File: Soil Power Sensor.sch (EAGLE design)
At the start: 91 parts, among them J1 12401832E402A, U10 TPS7A20330PDBVR, U11 TPS60403DBVR, U12 REF1933AIDDCR, U13 TLV1117LV33DCYR, U14 FSA2466UMX, U2 FT234XD-R, U3 MAX9944ATA+T, U4 ESP32-C3-MINI-1-N4, U5 LTC6362CDDPBF, U6 LTC6362CDDPBF, U7 INA296A5, U8 MAX11201AEUB+, U9 MAX11201AEUB+, X1 SMA-142-0701-801/806

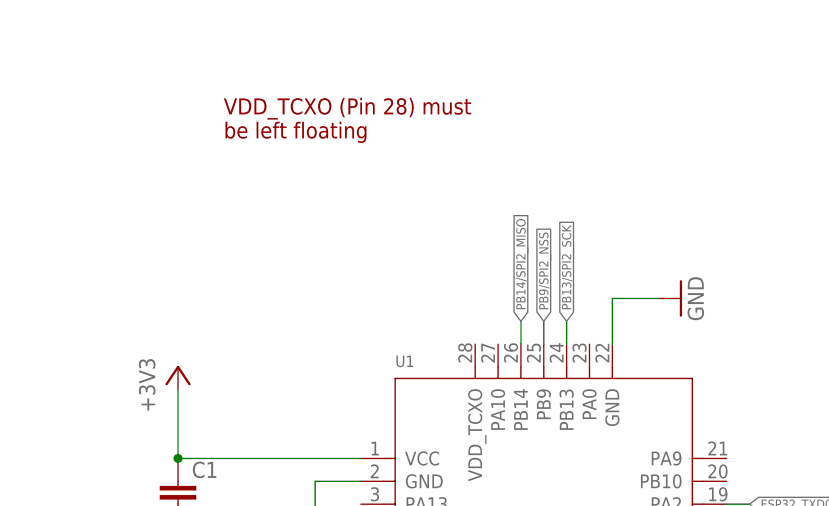
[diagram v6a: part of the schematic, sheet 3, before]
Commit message: Added voltage monitoring circuit
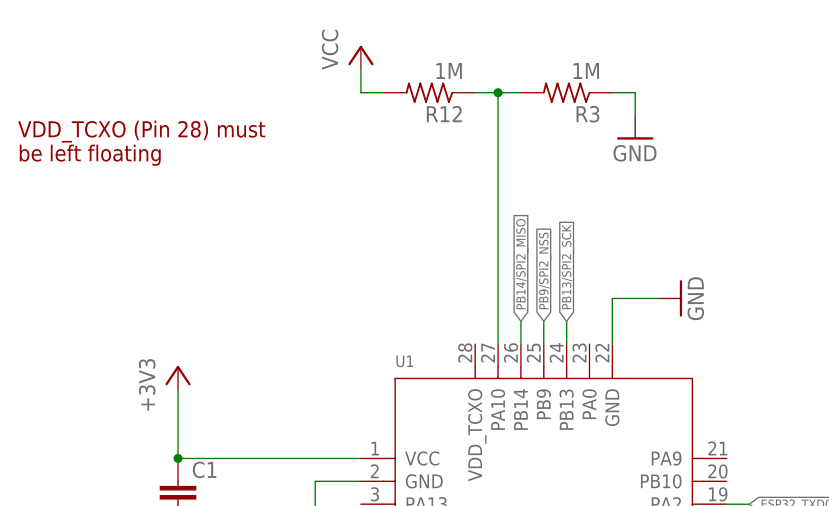
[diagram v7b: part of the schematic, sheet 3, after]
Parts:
- added R12, R3: 1M, rcl:R-US_R0603
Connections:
- new net N$34: R12.1, R3.2, U1.PA10
- net GND: now also R3.1
- net VCC: now also R12.2
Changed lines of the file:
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@@
 <part name="TP11" library="testpad" library_urn="urn:adsk.eagle:library:385" deviceset="TP" device="B1,27" package3d_urn="urn:adsk.eagle:package:27944/2"/>
 <part name="TP12" library="testpad" library_urn="urn:adsk.eagle:library:385" deviceset="TP" device="B1,27" package3d_urn="urn:adsk.eagle:package:27944/2"/>
+<part name="R3" library="rcl" library_urn="urn:adsk.eagle:library:334" deviceset="R-US_" device="R0603" package3d_urn="urn:adsk.eagle:package:23555/3" value="1M"/>
+<part name="R12" library="rcl" library_urn="urn:adsk.eagle:library:334" deviceset="R-US_" device="R0603" package3d_urn="urn:adsk.eagle:package:23555/3" value="1M"/>
+<part name="P+4" library="supply1" library_urn="urn:adsk.eagle:library:371" deviceset="VCC" device=""/>
+<part name="GND28" library="supply1" library_urn="urn:adsk.eagle:library:371" deviceset="GND" device=""/>
 </parts>
 <sheets>
@@
 <sheet>
 <plain>
-<text x="33.02" y="195.58" size="1.778" layer="94">VDD_TCXO (Pin 28) must
+<text x="10.16" y="193.04" size="1.778" layer="94">VDD_TCXO (Pin 28) must
 be left floating</text>
 <text x="86.36" y="119.38" size="1.778" layer="94">GNDs should be placed as close to components/pins as possible</text>
@@
 <attribute name="NAME" x="147.315559375" y="78.74148125" size="2.54148125" layer="95"/>
 <attribute name="VALUE" x="134.61003125" y="66.033359375" size="2.54331875" layer="96"/>
+</instance>
+<instance part="R3" gate="G$1" x="71.12" y="200.66" smashed="yes" rot="R180">
+<attribute name="NAME" x="74.93" y="199.1614" size="1.778" layer="95" rot="R180"/>
+<attribute name="VALUE" x="74.93" y="203.962" size="1.778" layer="96" rot="R180"/>
+</instance>
+<instance part="R12" gate="G$1" x="55.88" y="200.66" smashed="yes" rot="R180">
+<attribute name="NAME" x="59.69" y="199.1614" size="1.778" layer="95" rot="R180"/>
+<attribute name="VALUE" x="59.69" y="203.962" size="1.778" layer="96" rot="R180"/>
+</instance>
+<instance part="P+4" gate="VCC" x="48.26" y="205.74" smashed="yes">
+<attribute name="VALUE" x="45.72" y="203.2" size="1.778" layer="96" rot="R90"/>
+</instance>
+<instance part="GND28" gate="1" x="78.74" y="195.58" smashed="yes">
+<attribute name="VALUE" x="76.2" y="193.04" size="1.778" layer="96"/>
 </instance>
 </instances>
@@
 <wire x1="177.8" y1="63.5" x2="167.64" y2="63.5" width="0.1524" layer="91"/>
 <junction x="167.64" y="63.5"/>
+</segment>
+<segment>
+<pinref part="R3" gate="G$1" pin="1"/>
+<pinref part="GND28" gate="1" pin="GND"/>
+<wire x1="76.2" y1="200.66" x2="78.74" y2="200.66" width="0.1524" layer="91"/>
+<wire x1="78.74" y1="200.66" x2="78.74" y2="198.12" width="0.1524" layer="91"/>
 </segment>
 </net>
@@
 </segment>
 </net>
+<net name="N$34" class="0">
+<segment>
+<pinref part="R12" gate="G$1" pin="1"/>
+<pinref part="U1" gate="G$1" pin="PA10"/>
+<wire x1="60.96" y1="200.66" x2="63.5" y2="200.66" width="0.1524" layer="91"/>
+<wire x1="63.5" y1="200.66" x2="63.5" y2="172.72" width="0.1524" layer="91"/>
+<pinref part="R3" gate="G$1" pin="2"/>
+<wire x1="66.04" y1="200.66" x2="63.5" y2="200.66" width="0.1524" layer="91"/>
+<junction x="63.5" y="200.66"/>
+</segment>
+</net>
+<net name="VCC" class="0">
+<segment>
+<pinref part="P+4" gate="VCC" pin="VCC"/>
+<pinref part="R12" gate="G$1" pin="2"/>
+<wire x1="48.26" y1="203.2" x2="48.26" y2="200.66" width="0.1524" layer="91"/>
+<wire x1="48.26" y1="200.66" x2="50.8" y2="200.66" width="0.1524" layer="91"/>
+</segment>
+</net>

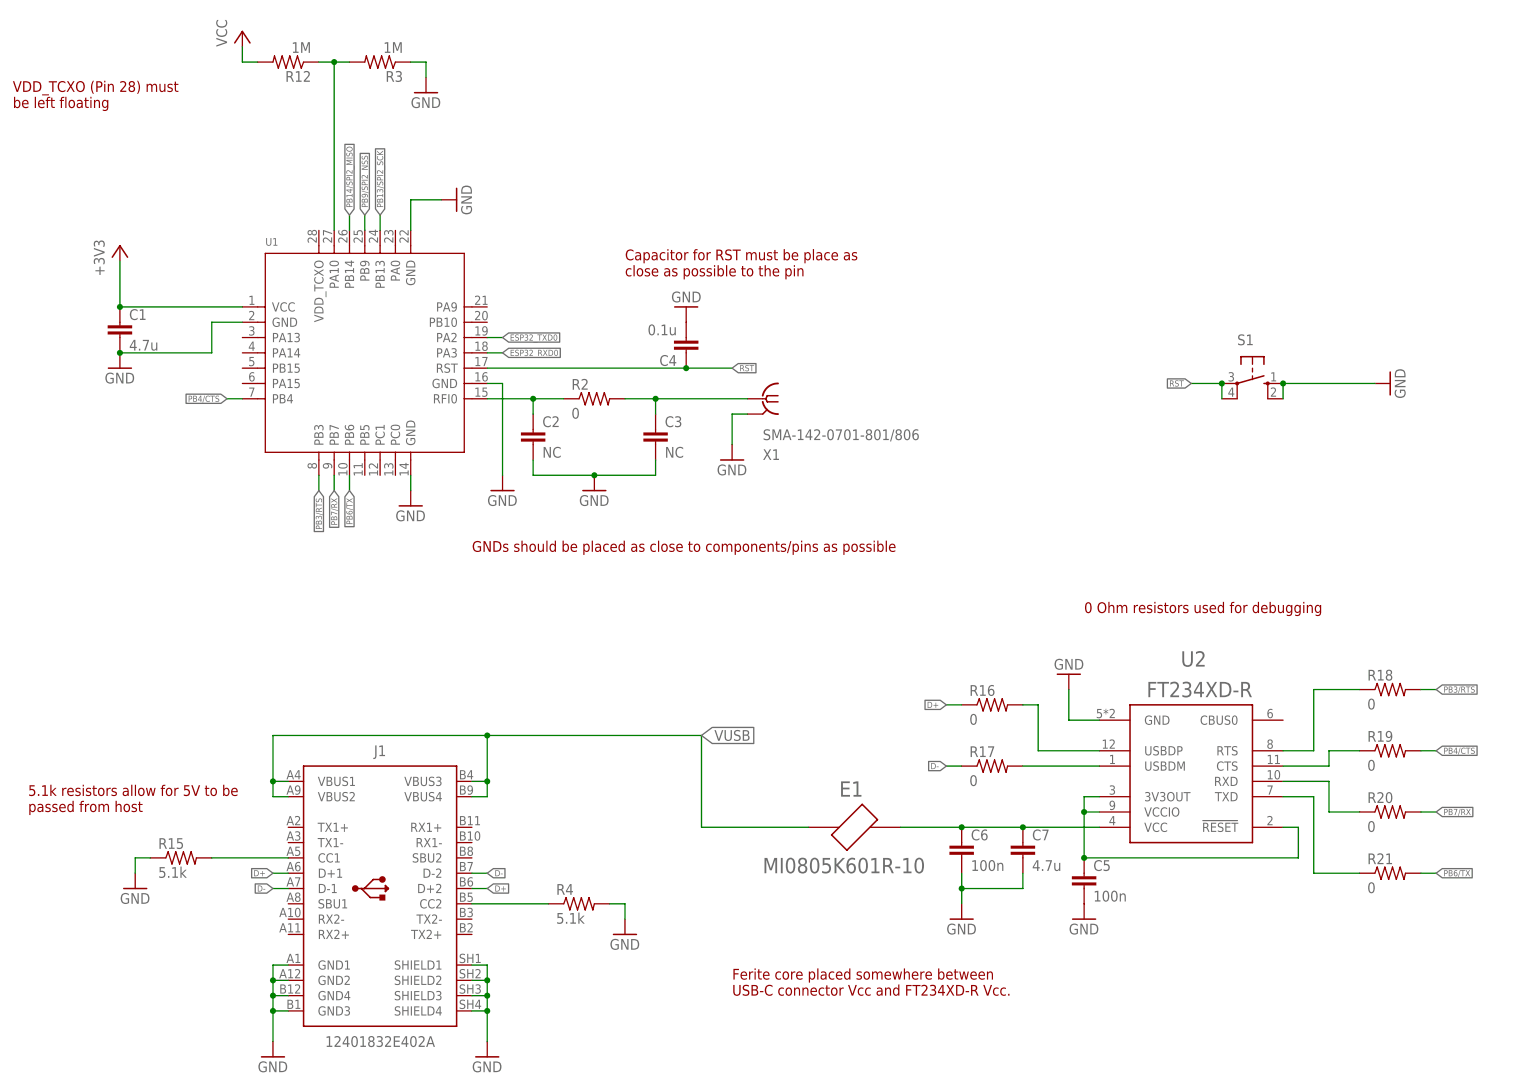
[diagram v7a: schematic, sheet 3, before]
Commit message: Added JTAG connection for STM32
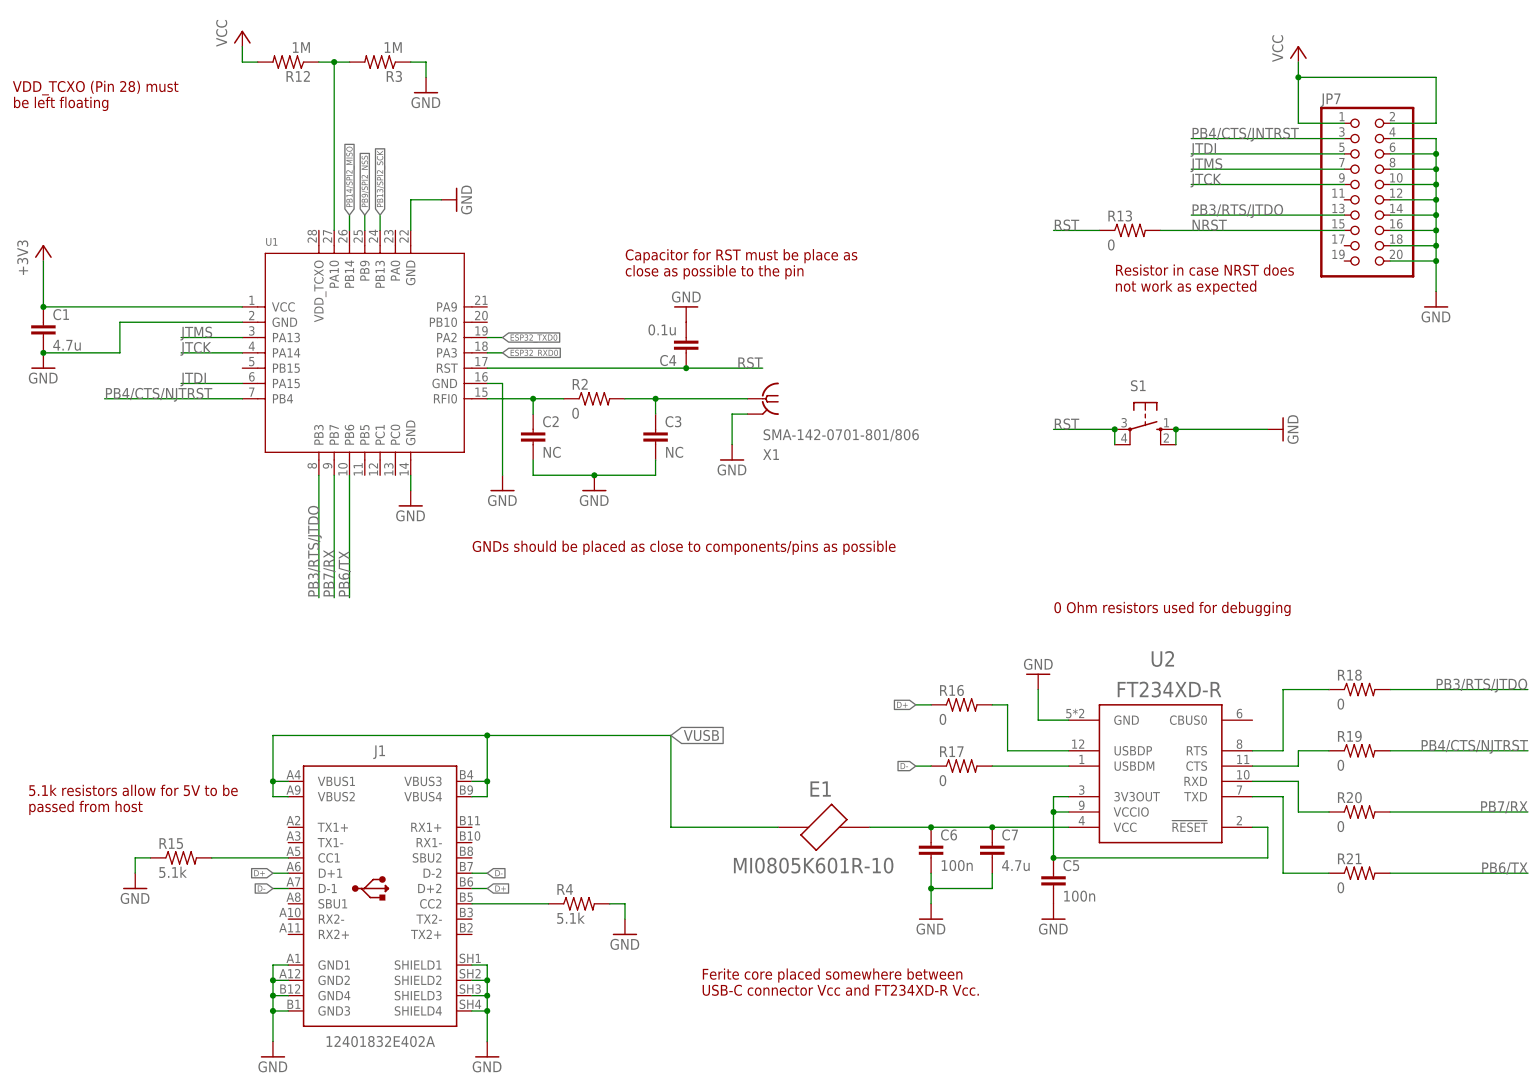
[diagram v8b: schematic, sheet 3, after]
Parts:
- added JP7: (no value), pinhead:PINHD-2X10
- added R13: 0, rcl:R-US_R0603
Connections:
- net PB4/CTS renamed PB4/CTS/NJTRST
- removed net PB3/RTS: R18.2, U1.PB3
- new net JTCK: JP7.9, U1.PA14
- new net JTDI: JP7.5, U1.PA15
- new net JTMS: JP7.7, U1.PA13
- new net NRST: JP7.15, R13.2
- new net PB3/RTS/JTDO: JP7.13, R18.2, U1.PB3
- new net PB4/CTS/JNTRST: JP7.3
- net GND: now also JP7.10, JP7.12, JP7.14, JP7.16, JP7.18, JP7.20, JP7.4, JP7.6, JP7.8
- net RST: now also R13.1
- net VCC: now also JP7.1, JP7.2
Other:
- note added: "Resistor in case NRST does not work as expected"
- moved on the sheet: C1, C5, C6, C7, E1, R16, R17, R18, R19, R20, R21, S1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
